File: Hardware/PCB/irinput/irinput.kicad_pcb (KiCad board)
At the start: 2 copper layers, 156 x 170.5 mm, 48 parts, among them J1 AudioJack3, J2 Synth_power_2x5, J3 AudioJack3, J4 Conn_01x06, J5 Conn_01x06, J6 AudioJack2, J7 AudioJack2, Q1 TOPS-050, Q2 TOPS-050, SW1 SW_DPDT_x2, SW2 SW_DPDT_x2, U1 TL074

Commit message: Corrections
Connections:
- U1 pad 2: /DC -> Net-(R3-Pad2)
- U1 pad 3: Net-(R3-Pad2) -> /DC
- U1 pad 5: Net-(RV2-Pad2) -> Net-(C1-Pad2)
- U1 pad 6: Net-(C1-Pad2) -> Net-(RV2-Pad2)
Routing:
- net /DC: track 112.0 -> 108.0 mm
- net Net-(RV2-Pad2): track 32.8 -> 30.2 mm
- net Net-(C1-Pad2): track 41.8 -> 44.3 mm
- net Net-(R3-Pad2): track 18.2 -> 18.7 mm
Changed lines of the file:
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@@
       (net 35 "Net-(R8-Pad1)") (pintype "output"))
     (pad "2" thru_hole oval locked (at 0 -2.54) (size 2.4 1.6) (drill 0.8) (layers *.Cu *.Mask)
-      (net 31 "/DC") (pinfunction "-") (pintype "input"))
+      (net 33 "Net-(R3-Pad2)") (pinfunction "-") (pintype "input"))
     (pad "3" thru_hole oval locked (at 0 -5.08) (size 2.4 1.6) (drill 0.8) (layers *.Cu *.Mask)
-      (net 33 "Net-(R3-Pad2)") (pinfunction "+") (pintype "input"))
+      (net 31 "/DC") (pinfunction "+") (pintype "input"))
     (pad "4" thru_hole oval locked (at 0 -7.62) (size 2.4 1.6) (drill 0.8) (layers *.Cu *.Mask)
       (net 1 "+12V") (pinfunction "V+") (pintype "power_in"))
     (pad "5" thru_hole oval locked (at 0 -10.16) (size 2.4 1.6) (drill 0.8) (layers *.Cu *.Mask)
-      (net 38 "Net-(RV2-Pad2)") (pinfunction "+") (pintype "input"))
+      (net 6 "Net-(C1-Pad2)") (pinfunction "+") (pintype "input"))
     (pad "6" thru_hole oval locked (at 0 -12.7) (size 2.4 1.6) (drill 0.8) (layers *.Cu *.Mask)
-      (net 6 "Net-(C1-Pad2)") (pinfunction "-") (pintype "input"))
+      (net 38 "Net-(RV2-Pad2)") (pinfunction "-") (pintype "input"))
     (pad "7" thru_hole oval locked (at 0 -15.24) (size 2.4 1.6) (drill 0.8) (layers *.Cu *.Mask)
       (net 36 "Net-(R9-Pad1)") (pintype "output"))
@@
   (segment (start 83.210489 96.226225) (end 83.210489 103.125489) (width 0.25) (layer "F.Cu") (net 6))
   (segment (start 82.26 82.22) (end 83.844021 83.804021) (width 0.25) (layer "F.Cu") (net 6))
-  (segment (start 91.53404 113.97) (end 93.655 113.97) (width 0.25) (layer "B.Cu") (net 6))
-  (segment (start 88.040489 110.476449) (end 91.53404 113.97) (width 0.25) (layer "B.Cu") (net 6))
-  (segment (start 85.085 105) (end 88.040489 107.955489) (width 0.25) (layer "B.Cu") (net 6))
-  (segment (start 93.655 113.97) (end 96.2 116.515) (width 0.25) (layer "B.Cu") (net 6))
-  (segment (start 88.040489 107.955489) (end 88.040489 110.476449) (width 0.25) (layer "B.Cu") (net 6))
+  (segment (start 91.649511 116.414511) (end 93.559511 116.414511) (width 0.25) (layer "B.Cu") (net 6))
+  (segment (start 85.085 105) (end 87.554 107.469) (width 0.25) (layer "B.Cu") (net 6))
+  (segment (start 87.554 112.319) (end 91.649511 116.414511) (width 0.25) (layer "B.Cu") (net 6))
+  (segment (start 87.554 107.469) (end 87.554 112.319) (width 0.25) (layer "B.Cu") (net 6))
+  (segment (start 93.559511 116.414511) (end 96.2 119.055) (width 0.25) (layer "B.Cu") (net 6))
   (segment (start 107.62 113.97) (end 107.62 119.05) (width 0.25) (layer "F.Cu") (net 7))
   (segment (start 103.82 113.975) (end 107.615 113.975) (width 0.25) (layer "B.Cu") (net 7))
+  (segment (start 81.045489 128.035489) (end 82.22 129.21) (width 0.25) (layer "B.Cu") (net 8))
+  (segment (start 81.077 123.61199) (end 81.045489 123.643501) (width 0.25) (layer "B.Cu") (net 8))
+  (segment (start 81.077 99.173) (end 81.077 123.61199) (width 0.25) (layer "B.Cu") (net 8))
+  (segment (start 111.21 65) (end 106.650978 65) (width 0.25) (layer "B.Cu") (net 8))
+  (segment (start 98.525489 73.125489) (end 98.525489 81.724511) (width 0.25) (layer "B.Cu") (net 8))
   (segment (start 106.650978 65) (end 98.525489 73.125489) (width 0.25) (layer "B.Cu") (net 8))
-  (segment (start 111.21 65) (end 106.650978 65) (width 0.25) (layer "B.Cu") (net 8))
-  (segment (start 98.525489 81.724511) (end 80.5 99.75) (width 0.25) (layer "B.Cu") (net 8))
-  (segment (start 98.525489 73.125489) (end 98.525489 81.724511) (width 0.25) (layer "B.Cu") (net 8))
-  (segment (start 80.5 99.75) (end 80.5 127.49) (width 0.25) (layer "B.Cu") (net 8))
-  (segment (start 80.5 127.49) (end 82.22 129.21) (width 0.25) (layer "B.Cu") (net 8))
+  (segment (start 81.045489 123.643501) (end 81.045489 128.035489) (width 0.25) (layer "B.Cu") (net 8))
+  (segment (start 98.525489 81.724511) (end 81.077 99.173) (width 0.25) (layer "B.Cu") (net 8))
   (segment (start 178.359 165.221) (end 181.35 162.23) (width 0.25) (layer "F.Cu") (net 10))
   (segment (start 175 178.735) (end 178.359 175.376) (width 0.25) (layer "F.Cu") (net 10))
@@
   (segment (start 87.26 98.125) (end 85.085 100.3) (width 0.25) (layer "F.Cu") (net 31))
   (segment (start 103.714511 49.295489) (end 101.809511 49.295489) (width 0.25) (layer "F.Cu") (net 31))
-  (segment (start 80.949511 115.559811) (end 92.0647 126.675) (width 0.25) (layer "B.Cu") (net 31))
+  (segment (start 85.085 100.3) (end 81.966 103.419) (width 0.25) (layer "B.Cu") (net 31))
+  (segment (start 90.186211 121.174211) (end 93.239211 121.174211) (width 0.25) (layer "B.Cu") (net 31))
+  (segment (start 88.062 119.05) (end 90.186211 121.174211) (width 0.25) (layer "B.Cu") (net 31))
+  (segment (start 81.966 109.901) (end 88.062 115.997) (width 0.25) (layer "B.Cu") (net 31))
+  (segment (start 81.966 103.419) (end 81.966 109.901) (width 0.25) (layer "B.Cu") (net 31))
   (segment (start 87.26 82.22) (end 98.69 70.79) (width 0.25) (layer "B.Cu") (net 31))
-  (segment (start 85.085 100.3) (end 80.949511 104.435489) (width 0.25) (layer "B.Cu") (net 31))
+  (segment (start 88.062 115.997) (end 88.062 119.05) (width 0.25) (layer "B.Cu") (net 31))
   (segment (start 98.69 70.79) (end 98.73 70.79) (width 0.25) (layer "B.Cu") (net 31))
-  (segment (start 92.0647 126.675) (end 96.2 126.675) (width 0.25) (layer "B.Cu") (net 31))
-  (segment (start 80.949511 104.435489) (end 80.949511 115.559811) (width 0.25) (layer "B.Cu") (net 31))
+  (segment (start 93.239211 121.174211) (end 96.2 124.135) (width 0.25) (layer "B.Cu") (net 31))
   (segment (start 92.38 97.835) (end 89.915 100.3) (width 0.25) (layer "F.Cu") (net 32))
   (segment (start 92.38 94.92) (end 92.38 97.835) (width 0.25) (layer "F.Cu") (net 32))
-  (segment (start 90.221 124.13) (end 92.38 124.13) (width 0.25) (layer "B.Cu") (net 33))
-  (segment (start 82.22 116.129) (end 90.221 124.13) (width 0.25) (layer "B.Cu") (net 33))
-  (segment (start 96.195 124.13) (end 96.2 124.135) (width 0.25) (layer "B.Cu") (net 33))
-  (segment (start 92.38 124.13) (end 96.195 124.13) (width 0.25) (layer "B.Cu") (net 33))
-  (segment (start 82.22 115.24) (end 82.22 116.129) (width 0.25) (layer "B.Cu") (net 33))
+  (segment (start 82.22 115.24) (end 91.11 124.13) (width 0.25) (layer "F.Cu") (net 33))
+  (segment (start 91.11 124.13) (end 92.38 124.13) (width 0.25) (layer "F.Cu") (net 33))
+  (segment (start 93.655 124.13) (end 96.2 126.675) (width 0.25) (layer "B.Cu") (net 33))
+  (segment (start 92.38 124.13) (end 93.655 124.13) (width 0.25) (layer "B.Cu") (net 33))
   (segment (start 95.73 109.7) (end 96.19 110.16) (width 0.25) (layer "B.Cu") (net 34))
   (segment (start 89.915 109.7) (end 95.73 109.7) (width 0.25) (layer "B.Cu") (net 34))
   (segment (start 92.38 129.21) (end 96.195 129.21) (width 0.25) (layer "B.Cu") (net 35))
   (segment (start 103.683 104.317) (end 105 103) (width 0.25) (layer "F.Cu") (net 36))
+  (segment (start 96.2 113.975) (end 98.0265 113.975) (width 0.25) (layer "F.Cu") (net 36))
+  (segment (start 98.0265 113.975) (end 103.683 108.3185) (width 0.25) (layer "F.Cu") (net 36))
   (segment (start 105 103) (end 105 102.5) (width 0.25) (layer "F.Cu") (net 36))
-  (segment (start 96.2 113.975) (end 97.836 113.975) (width 0.25) (layer "F.Cu") (net 36))
+  (segment (start 103.683 108.3185) (end 103.683 104.317) (width 0.25) (layer "F.Cu") (net 36))
   (segment (start 103.82 124.135) (end 102.159 122.474) (width 0.25) (layer "F.Cu") (net 36))
   (segment (start 102.159 120.716) (end 103.82 119.055) (width 0.25) (layer "F.Cu") (net 36))
-  (segment (start 97.836 113.975) (end 103.683 108.128) (width 0.25) (layer "F.Cu") (net 36))
-  (segment (start 103.683 108.128) (end 103.683 104.317) (width 0.25) (layer "F.Cu") (net 36))
   (segment (start 102.159 122.474) (end 102.159 120.716) (width 0.25) (layer "F.Cu") (net 36))
   (segment (start 102.23 125.725) (end 103.82 124.135) (width 0.25) (layer "B.Cu") (net 36))
@@
   (segment (start 95 147.5) (end 96.7 147.5) (width 0.25) (layer "B.Cu") (net 37))
   (segment (start 96.7 147.5) (end 98.73 149.53) (width 0.25) (layer "B.Cu") (net 37))
-  (segment (start 97.72452 117.53048) (end 97.72452 114.77548) (width 0.25) (layer "F.Cu") (net 38))
   (segment (start 105 105) (end 105 107.5) (width 0.25) (layer "F.Cu") (net 38))
-  (segment (start 96.2 119.055) (end 97.72452 117.53048) (width 0.25) (layer "F.Cu") (net 38))
-  (segment (start 97.72452 114.77548) (end 105 107.5) (width 0.25) (layer "F.Cu") (net 38))
+  (segment (start 105 107.715) (end 105 107.5) (width 0.25) (layer "F.Cu") (net 38))
+  (segment (start 96.2 116.515) (end 105 107.715) (width 0.25) (layer "F.Cu") (net 38))
   (segment (start 89.915 105) (end 105 105) (width 0.25) (layer "B.Cu") (net 38))
   (zone (net 2) (net_name "GND") (layers F&B.Cu) (hatch edge 0.508)

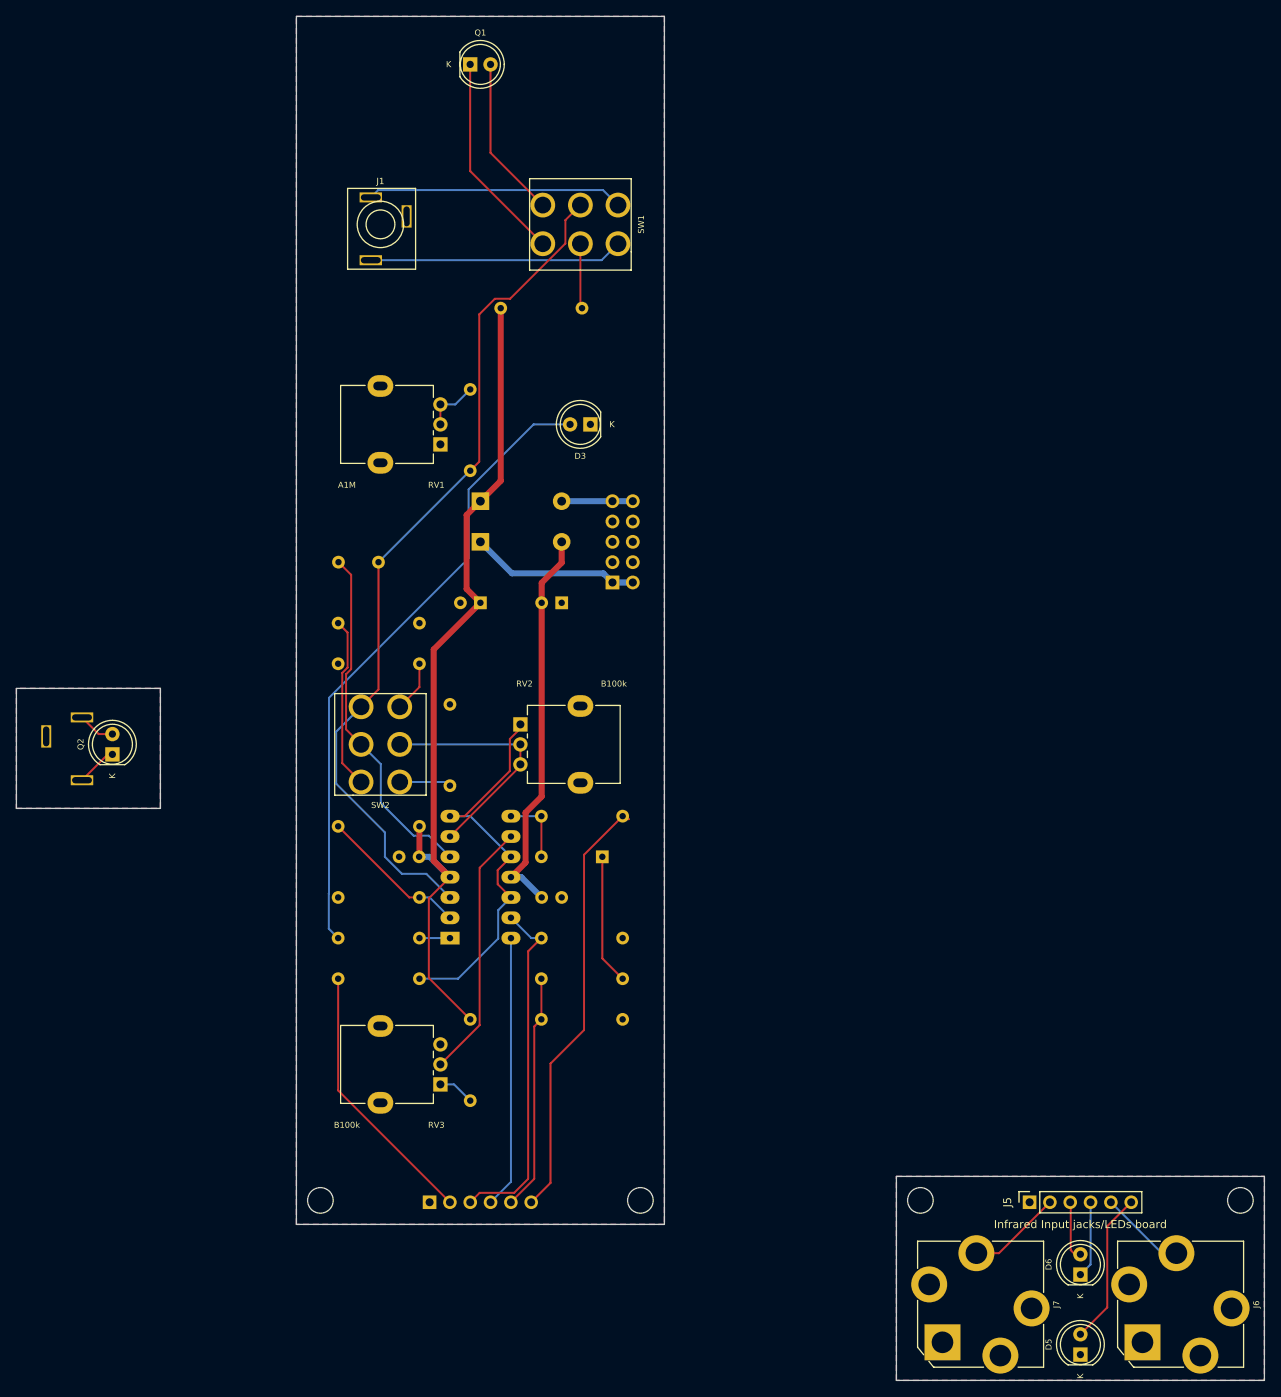
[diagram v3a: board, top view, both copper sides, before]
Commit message: Silkscreen cleanup, revised panel
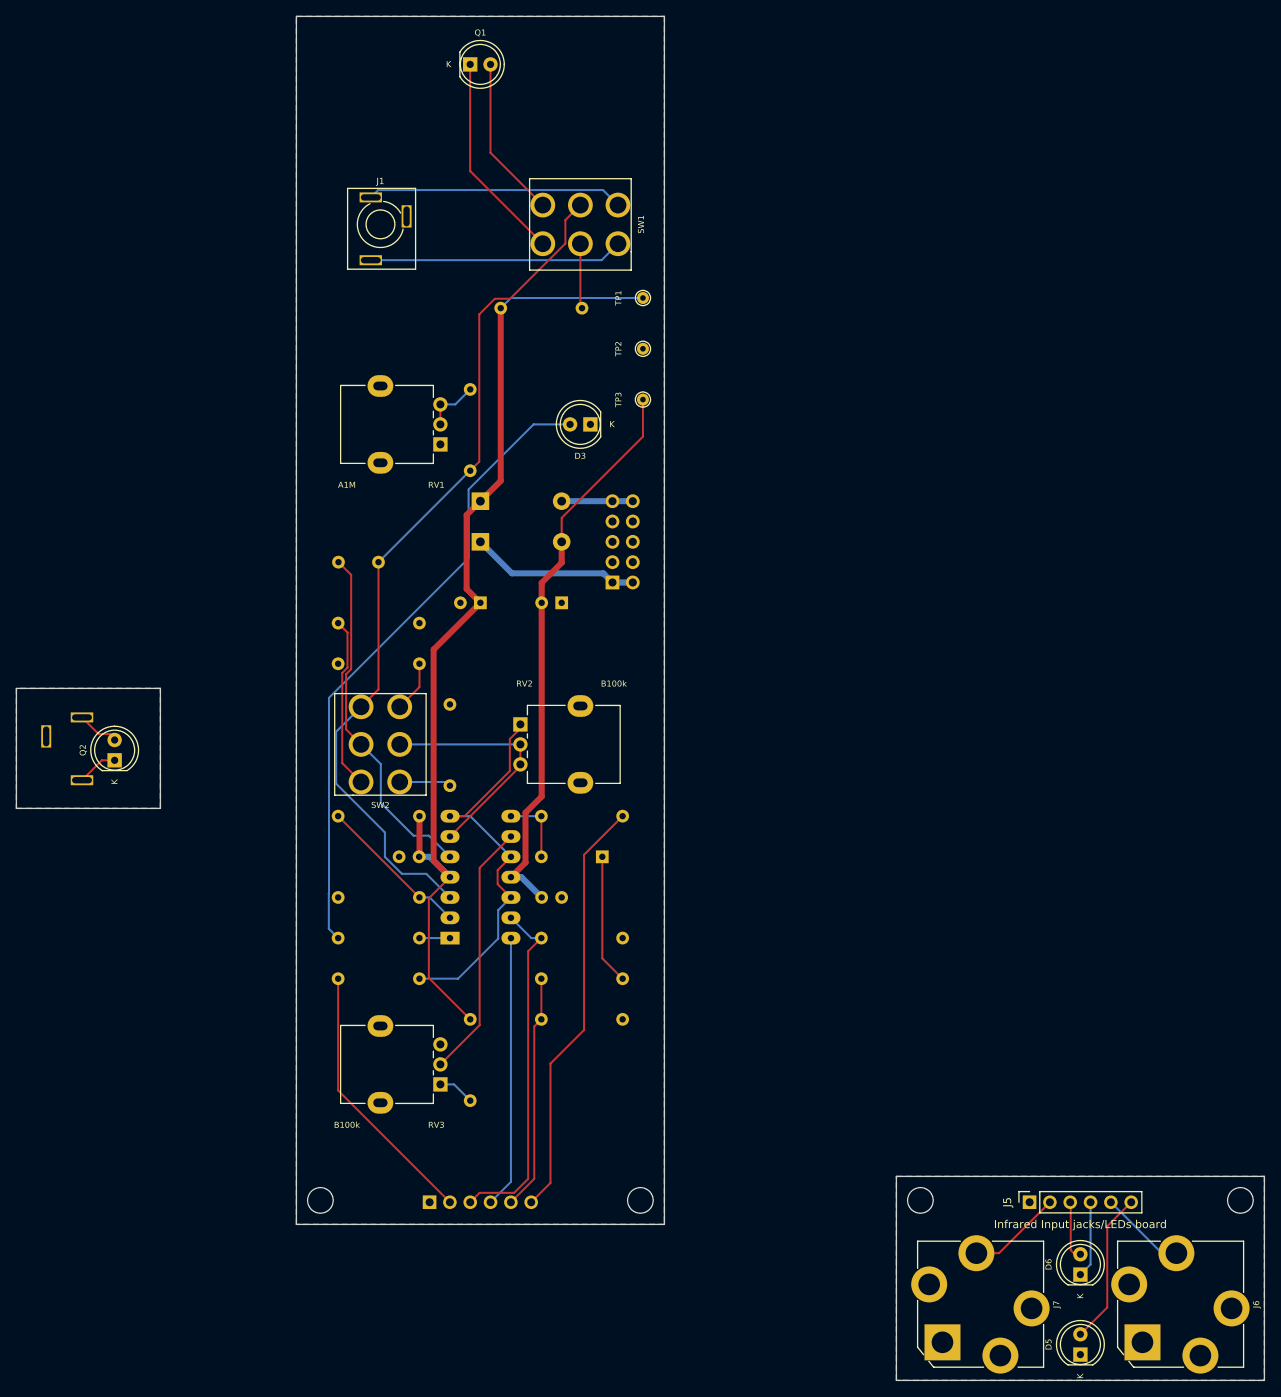
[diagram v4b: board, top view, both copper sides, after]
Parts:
- added TP1: +12V, ao_tht:TestPoint_THTPad_D1.5mm_Drill0.7mm, F.Cu at (120.3, 49.2)
- added TP2: GND, ao_tht:TestPoint_THTPad_D1.5mm_Drill0.7mm, F.Cu at (120.3, 55.5)
- added TP3: -12V, ao_tht:TestPoint_THTPad_D1.5mm_Drill0.7mm, F.Cu at (120.3, 61.9)
- C1: value 1uF -> 100nF; footprint ao_tht:C_Rect_L7.2mm_W7.2mm_P5.00mm_FKS2_FKP2_MKS2_MKP2 -> ao_tht:C_Rect_L7.2mm_W2.5mm_P5.00mm_FKS2_FKP2_MKS2_MKP2
- moved R6 1.27 mm to (82.2, 114.0)
- moved Q2 0.79 mm to (54.3, 107.0)
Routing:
- net -12V: track 49.4 -> 71.4 mm
- net +12V: track 106.6 -> 126.1 mm
- net /GATE_LED: track 54.4 -> 53.0 mm
- net /CV_LED_2_P: track 7.36 -> 6.66 mm
- net Net-(R7-Pad1): track 6.47 -> 5.81 mm
- net Net-(R3-Pad2): track 18.7 -> 19.2 mm
- net Net-(R9-Pad1): track 50.1 -> 49.6 mm
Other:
- board text added: "CV LED 1"
- board text added: "CV LED 2"
- board text added: "CV OUT"
- board text added: "GATE LED"
- board text added: "GATE OUT"
- board text added: "GND"

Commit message: Catch up to 1st fab run version
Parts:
- removed B2: Board, ao_tht:Board_Marker
- removed J3: AudioJack3, ao_tht:Jack_3.5mm_PJ-301CM
- removed Q2: TOPS-050, ao_tht:LED_D5.0mm
- moved B1 0.07 mm to (92.4, 14.0)
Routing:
- net Net-(J3-PadT): track 5.11 -> 0.00 mm
- net Net-(J3-PadR): track 4.66 -> 0.00 mm
- removed copper zone on B.Cu, net GND2
- removed copper zone on F.Cu, net GND2
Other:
- board size 156 x 170.5 mm -> 121 x 170.5 mm
- board text added: "There is no Board B2!"
